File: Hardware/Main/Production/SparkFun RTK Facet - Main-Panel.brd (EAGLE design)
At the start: 140.6 x 187.7 mm, 990 parts, among them J1 QWIIC_RIGHT_ANGLE, J16 QWIIC_RIGHT_ANGLE, J2 U.FL, J21 CORTEX_JTAG_DEBUG_PTH, J24 U.FL, J28 QWIIC_RIGHT_ANGLE, J32 CORTEX_JTAG_DEBUG_PTH, J35 U.FL, J39 QWIIC_RIGHT_ANGLE, J43 CORTEX_JTAG_DEBUG_PTH, J46 U.FL, J50 QWIIC_RIGHT_ANGLE, J54 CORTEX_JTAG_DEBUG_PTH, J57 U.FL, J6 U.FL, J61 QWIIC_RIGHT_ANGLE, J65 CORTEX_JTAG_DEBUG_PTH, J68 U.FL, J72 QWIIC_RIGHT_ANGLE, J76 CORTEX_JTAG_DEBUG_PTH, J79 U.FL, J83 QWIIC_RIGHT_ANGLE, J87 CORTEX_JTAG_DEBUG_PTH, J9 CORTEX_JTAG_DEBUG_PTH, Q1 MBT3904DW1T1, Q10 SIL2308, Q11 MBT3904DW1T1, Q12 SIL2308, Q13 MBT3904DW1T1, Q14 SIL2308, Q15 MBT3904DW1T1, Q16 SIL2308, Q2 MBT3904DW1T1, Q3 SIL2308, Q4 SIL2308, Q5 MBT3904DW1T1, Q6 SIL2308, Q7 MBT3904DW1T1, Q8 SIL2308, Q9 MBT3904DW1T1, U1 74HC4052D, U10 MCP73833, U11 U-BLOX_ZED-F9P, U12 AP2112K-3.3, U13 CH340C, U14 MAX17048, U15 MCP73833, U16 74HC4052D, U17 STLQ015, U18 AP2112K-3.3, U19 USB251XB, U2 3.3V, U20 ESP-WROOM-3232D-NARROW, U21 3.3V, U22 U-BLOX_ZED-F9P, U23 CH340C, U24 MAX17048, U25 MCP73833, U26 74HC4052D, U27 STLQ015, U28 AP2112K-3.3, U29 USB251XB, U3 U-BLOX_ZED-F9P, U30 ESP-WROOM-3232D-NARROW, U31 3.3V, U32 U-BLOX_ZED-F9P, U33 CH340C, U34 MAX17048, U35 MCP73833, U36 74HC4052D, U37 STLQ015, U38 AP2112K-3.3, U39 USB251XB, U4 STLQ015, U40 ESP-WROOM-3232D-NARROW, U41 3.3V, U42 U-BLOX_ZED-F9P, U43 CH340C, U44 MAX17048, U45 MCP73833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

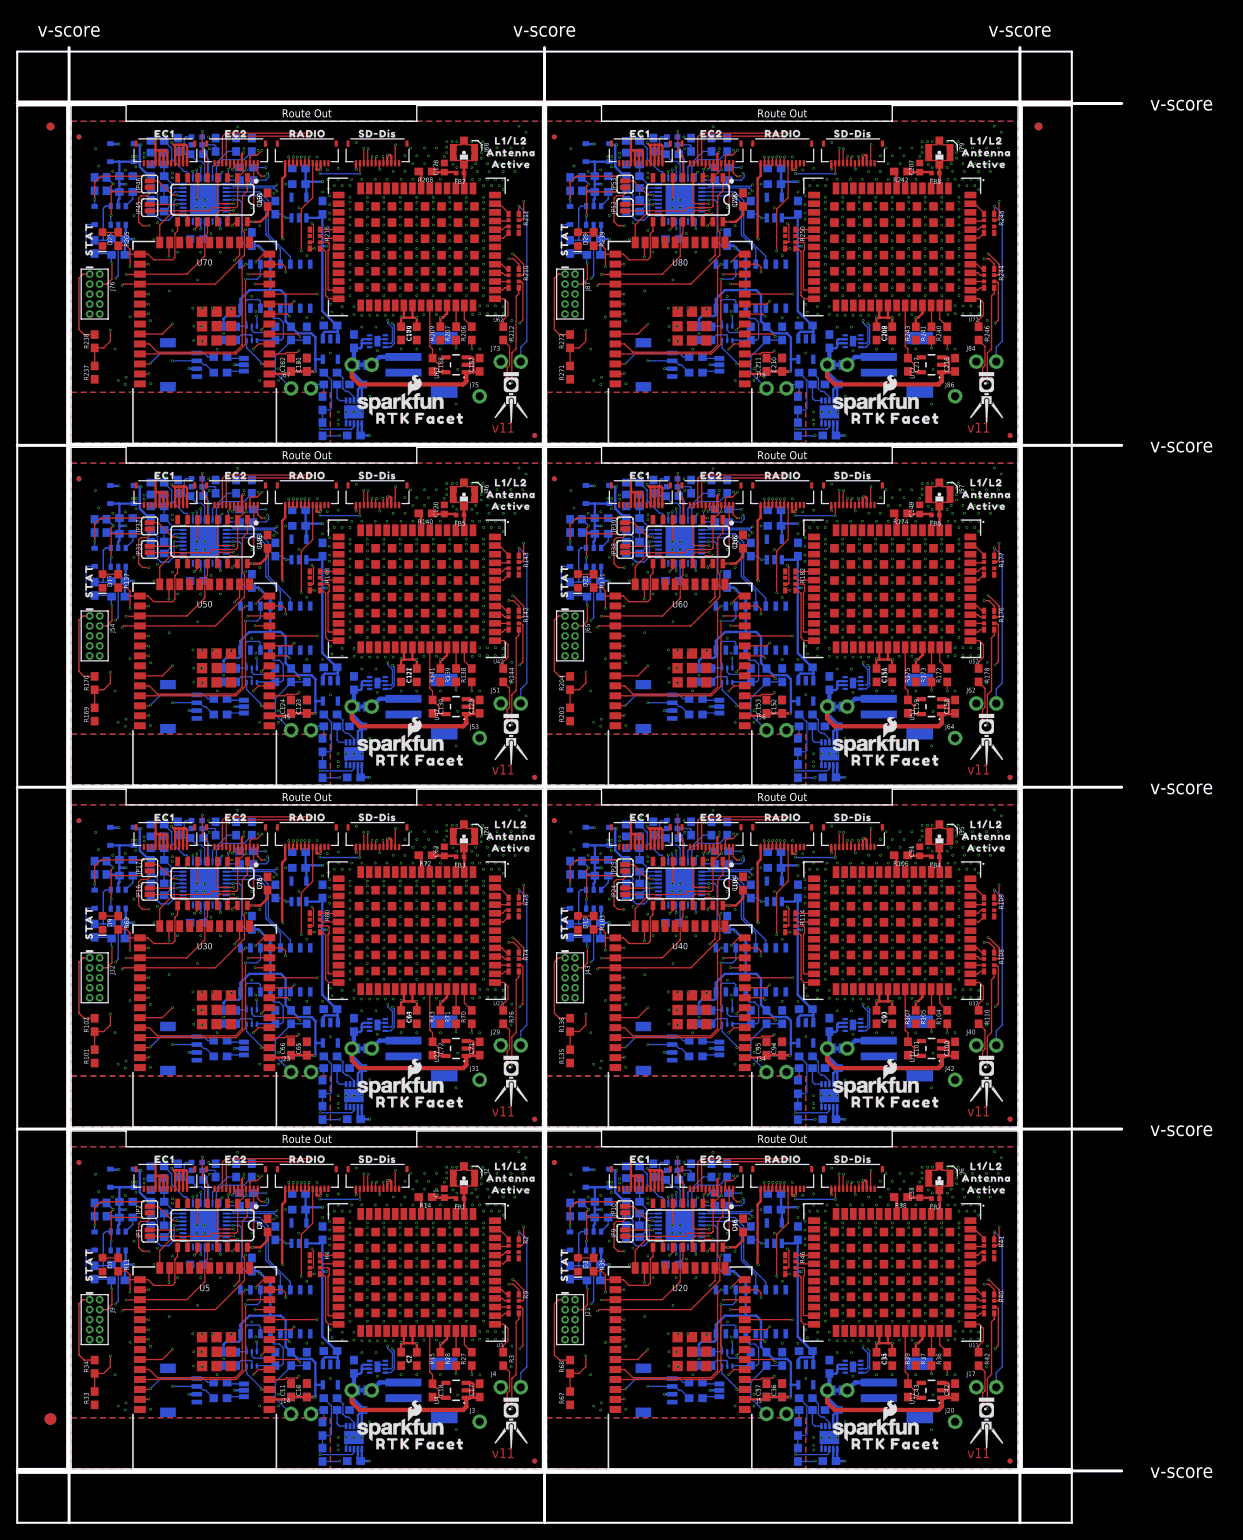
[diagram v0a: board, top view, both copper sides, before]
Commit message: Reduce Main, Connector, Display, and Cell board widths by 1mm to allow for v-score protrusion.
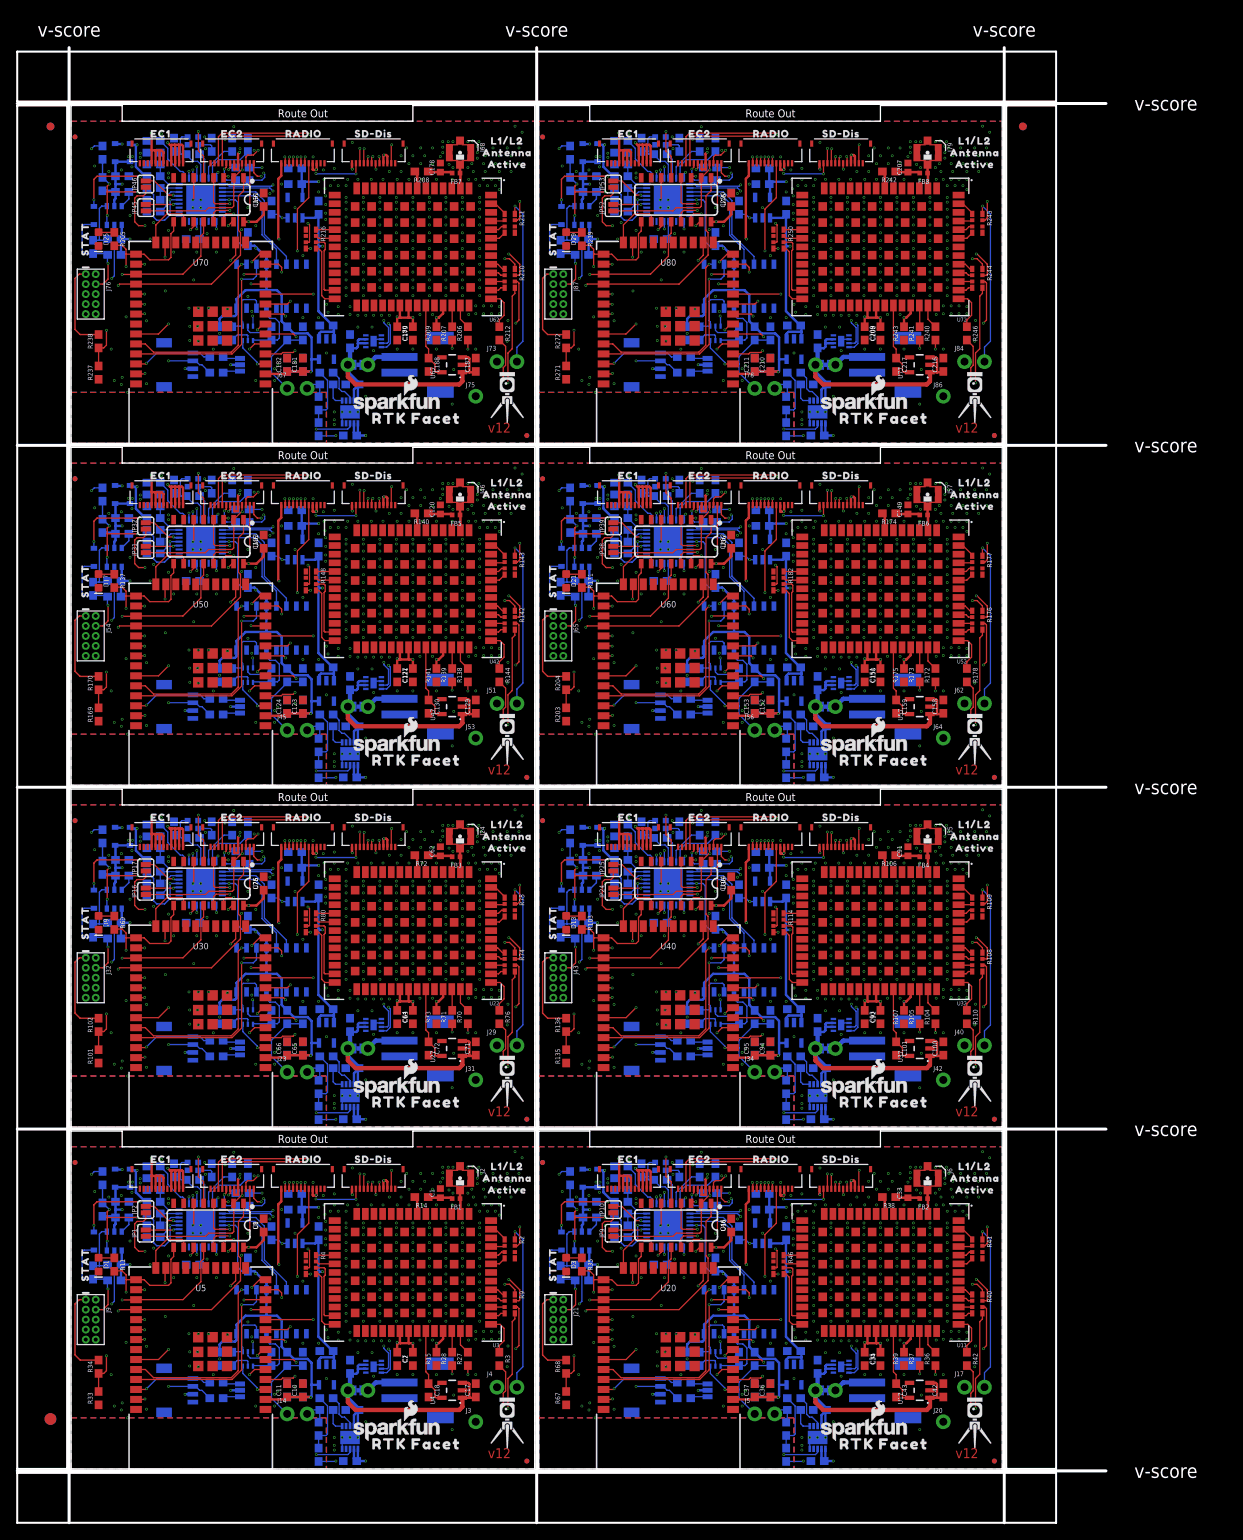
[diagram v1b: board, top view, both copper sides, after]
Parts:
- moved C136 4.12 mm to (4.00, 124.0), turned to 270 degrees
- moved C194 4.12 mm to (4.00, 167.5), turned to 270 degrees
- moved C23 4.12 mm to (4.00, 37.0), turned to 270 degrees
- moved C78 4.12 mm to (4.00, 80.5), turned to 270 degrees
- moved C107 4.00 mm to (63.5, 80.5), turned to 270 degrees
- moved C165 4.00 mm to (63.5, 124.0), turned to 270 degrees
- moved C223 4.00 mm to (63.5, 167.5), turned to 270 degrees
- moved C49 4.00 mm to (63.5, 37.0), turned to 270 degrees
- moved JP18 2.00 mm to (117.5, 44.5)
- moved JP20 2.00 mm to (117.5, 44.5)
- moved JP3 2.00 mm to (117.5, 1.00)
- moved JP33 2.00 mm to (117.5, 88.0)
- moved JP35 2.00 mm to (117.5, 88.0)
- moved JP47 2.00 mm to (117.5, 131.5)
- moved JP49 2.00 mm to (117.5, 131.5)
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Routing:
- net V_RAW6: track 78.3 -> 77.2 mm
- net V_RAW: track 78.3 -> 77.2 mm
- net V_RAW7: track 78.3 -> 77.2 mm
- net V_RAW4: track 78.3 -> 77.2 mm
- net V_RAW3: track 78.3 -> 77.2 mm
- net V_RAW2: track 78.3 -> 77.2 mm
- net V_RAW1: track 78.3 -> 77.2 mm
- net V_RAW5: track 78.3 -> 77.2 mm
- net ESP_3V7: track 118.6 -> 119.6 mm
- net ESP_3V5: track 118.6 -> 119.6 mm
- net ESP_3V3: track 118.6 -> 119.6 mm
- net ESP_3V2: track 118.6 -> 119.6 mm
- net ESP_3V1: track 118.6 -> 119.6 mm
- net ESP_3V4: track 118.6 -> 119.6 mm
- net ESP_3V6: track 118.6 -> 119.6 mm
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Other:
- board size 140.6 x 187.7 mm -> 138.6 x 187.7 mm
- board text added: "v12"
- board text removed: "v11"

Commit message: Add panel files for main v12, connector v12, display v14
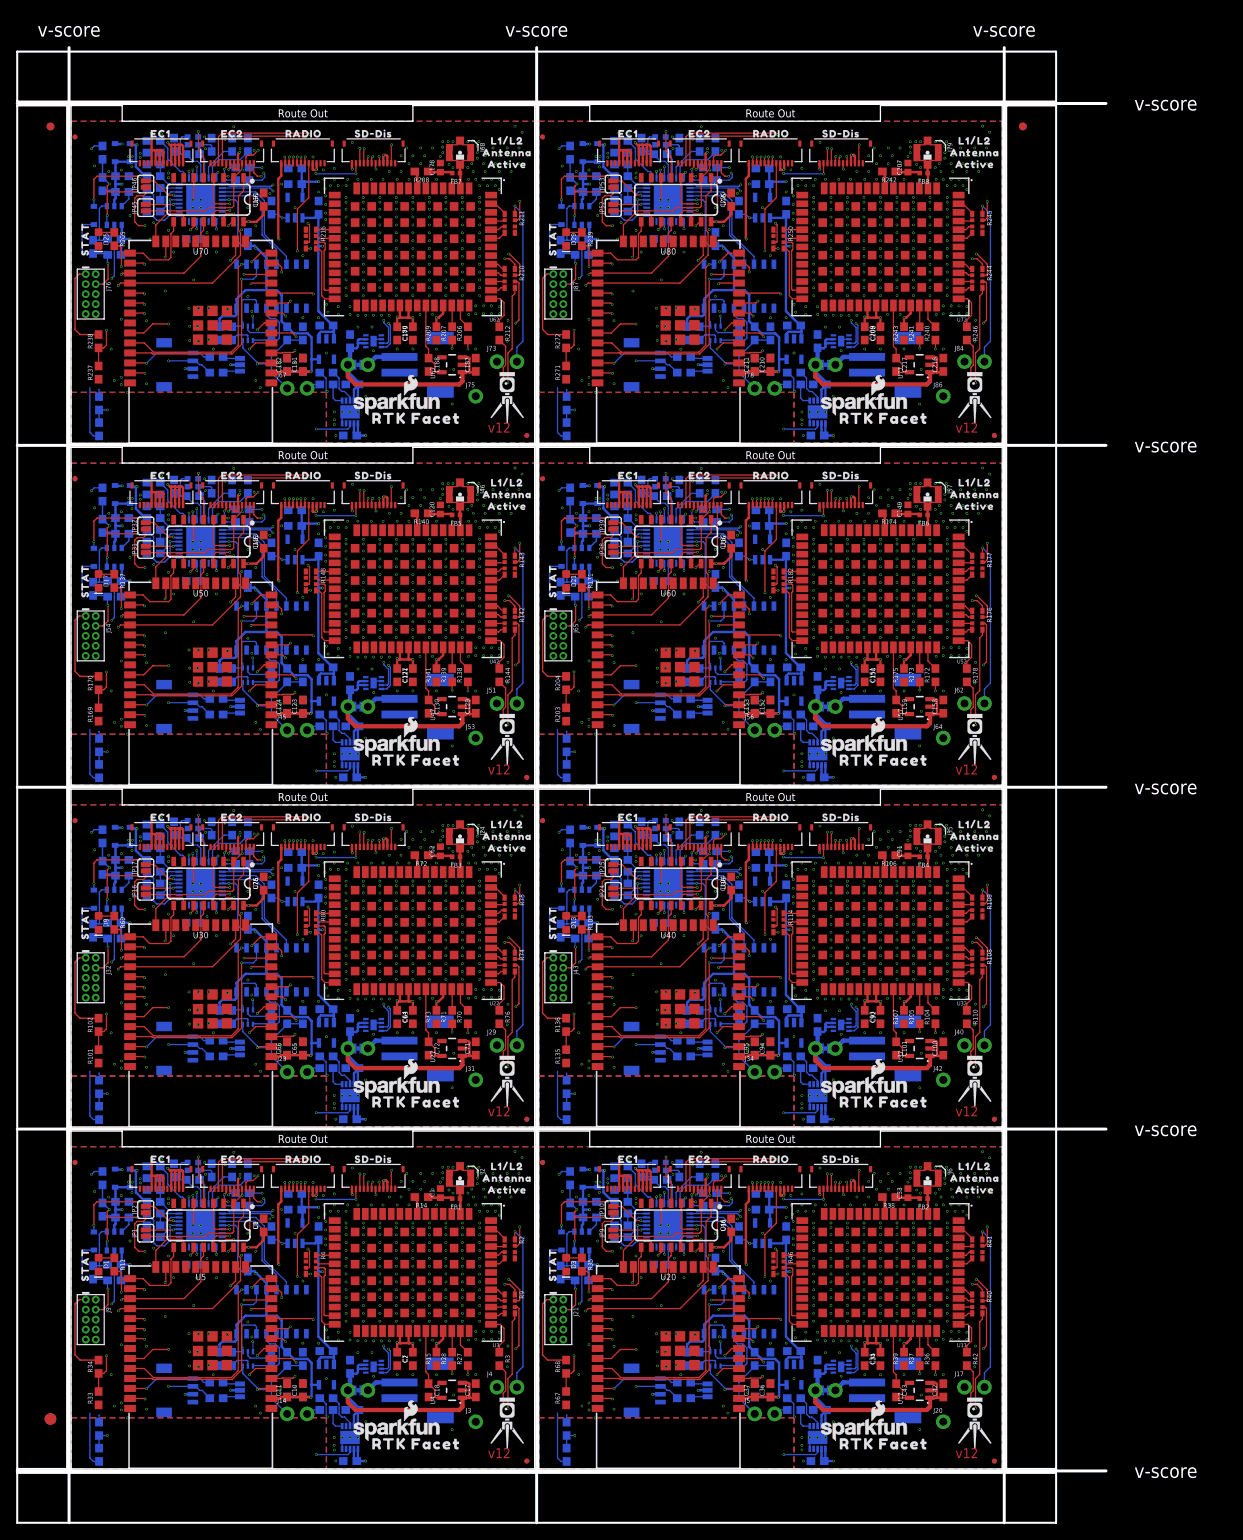
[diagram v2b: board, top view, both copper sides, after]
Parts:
- U20, U30, U40, U5, U50, U60, U70, U80: value ESP-WROOM-3232D-NARROW -> ESP-WROOM-3232D; device SparkFun-RF:ESP-WROOM-32D-NARROW -> SparkFun-RF:ESP-WROOM-32D
- moved R116 27.9 mm to (63.1, 48.6)
- moved R118 27.9 mm to (63.1, 45.3)
- moved R184 27.9 mm to (63.1, 92.1)
- moved R186 27.9 mm to (63.1, 88.8)
- moved R252 27.9 mm to (63.1, 135.6)
- moved R254 27.9 mm to (63.1, 132.3)
- moved R48 27.9 mm to (63.1, 5.10)
- moved R50 27.9 mm to (63.1, 1.80)
- moved R10 27.9 mm to (3.56, 1.80)
- moved R150 27.9 mm to (3.56, 92.1)
- moved R152 27.9 mm to (3.56, 88.8)
- moved R218 27.9 mm to (3.56, 135.6)
- moved R220 27.9 mm to (3.56, 132.3)
- moved R30 27.9 mm to (3.56, 5.10)
- moved R82 27.9 mm to (3.56, 48.6)
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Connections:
- net GND: now also U5.GND; no longer U5.GND1
- net GND1: now also U20.GND; no longer U20.GND1
- net GND2: now also U30.GND; no longer U30.GND1
- net GND3: now also U40.GND; no longer U40.GND1
- net GND4: now also U50.GND; no longer U50.GND1
- net GND5: now also U60.GND; no longer U60.GND1
- net GND6: now also U70.GND; no longer U70.GND1
- net GND7: now also U80.GND; no longer U80.GND1
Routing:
- net CHG_THERM8: track 7.78 -> 34.5 mm, vias 0 -> 2
- net CHG_THERM7: track 7.78 -> 34.5 mm, vias 0 -> 2
- net CHG_THERM5: track 7.78 -> 34.5 mm, vias 0 -> 2
- net CHG_THERM4: track 7.78 -> 34.5 mm, vias 0 -> 2
- net CHG_THERM6: track 7.78 -> 34.5 mm, vias 0 -> 2
- net CHG_THERM3: track 7.78 -> 34.5 mm, vias 0 -> 2
- net CHG_THERM2: track 7.78 -> 34.5 mm, vias 0 -> 2
- net CHG_THERM1: track 7.78 -> 34.5 mm, vias 0 -> 2
- net GND7: track 14.9 -> 19.1 mm
- net GND6: track 14.9 -> 19.1 mm
- net GND5: track 14.9 -> 19.1 mm
- net GND1: track 14.9 -> 19.1 mm
- net GND3: track 14.9 -> 19.1 mm
- net GND4: track 14.9 -> 19.1 mm
- net GND: track 14.9 -> 19.1 mm
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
